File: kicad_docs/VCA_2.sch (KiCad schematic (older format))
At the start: 16 parts, among them U1 SSM2164, U2 TL072, U3 TL072, U4 TL072

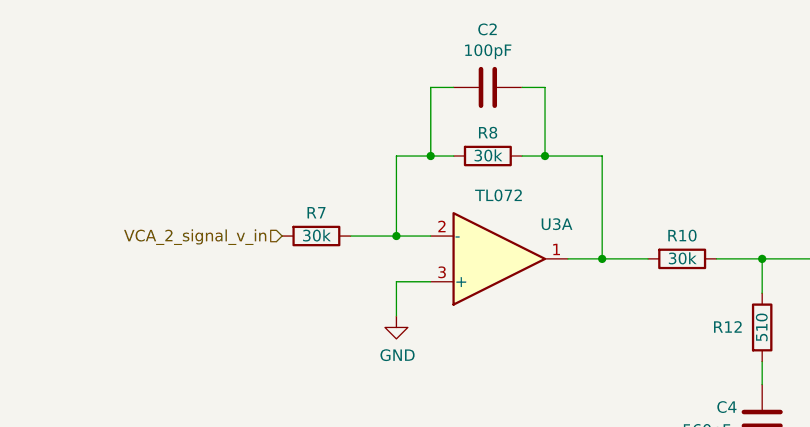
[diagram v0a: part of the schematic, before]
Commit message: add AC/DC coupling caps and jumper
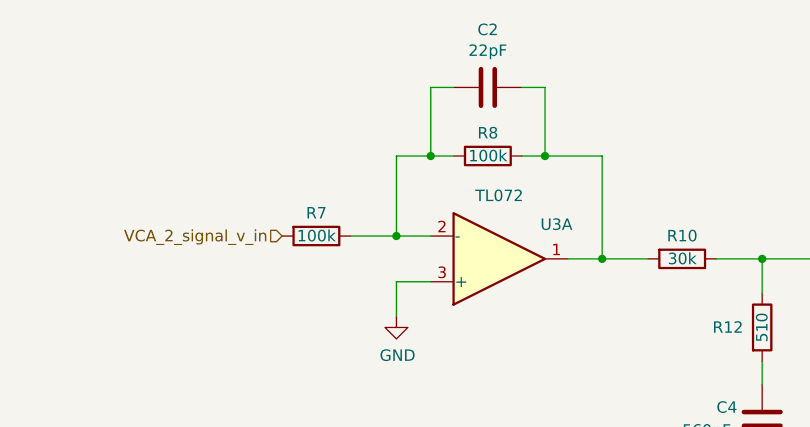
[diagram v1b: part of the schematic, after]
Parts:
- C2: value 100pF -> 22pF
- R7, R8: value 30k -> 100k
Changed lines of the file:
@@
 AR Path="/5E4A03B7/5E985A8F" Ref="R8"  Part="1"
 F 0 "R8" V 4600 2150 50  0000 C CNN
-F 1 "30k" V 4700 2150 50  0000 C CNN
+F 1 "100k" V 4700 2150 50  0000 C CNN
 F 2 "Resistor_SMD:R_0805_2012Metric_Pad1.15x1.40mm_HandSolder" V 4630 2150 50  0001 C CNN
 F 3 "~" H 4700 2150 50  0001 C CNN
@@
 AR Path="/5E4A03B7/5E985AA7" Ref="R7"  Part="1"
 F 0 "R7" V 3850 2500 50  0000 C CNN
-F 1 "30k" V 3950 2500 50  0000 C CNN
+F 1 "100k" V 3950 2500 50  0000 C CNN
 F 2 "Resistor_SMD:R_0805_2012Metric_Pad1.15x1.40mm_HandSolder" V 3880 2500 50  0001 C CNN
 F 3 "~" H 3950 2500 50  0001 C CNN
@@
 AR Path="/5E4A03B7/5E985ABB" Ref="C2"  Part="1"
 F 0 "C2" V 4448 1850 50  0000 C CNN
-F 1 "100pF" V 4539 1850 50  0000 C CNN
+F 1 "22pF" V 4539 1850 50  0000 C CNN
 F 2 "Capacitor_SMD:C_0805_2012Metric_Pad1.15x1.40mm_HandSolder" H 4738 1700 50  0001 C CNN
 F 3 "~" H 4700 1850 50  0001 C CNN

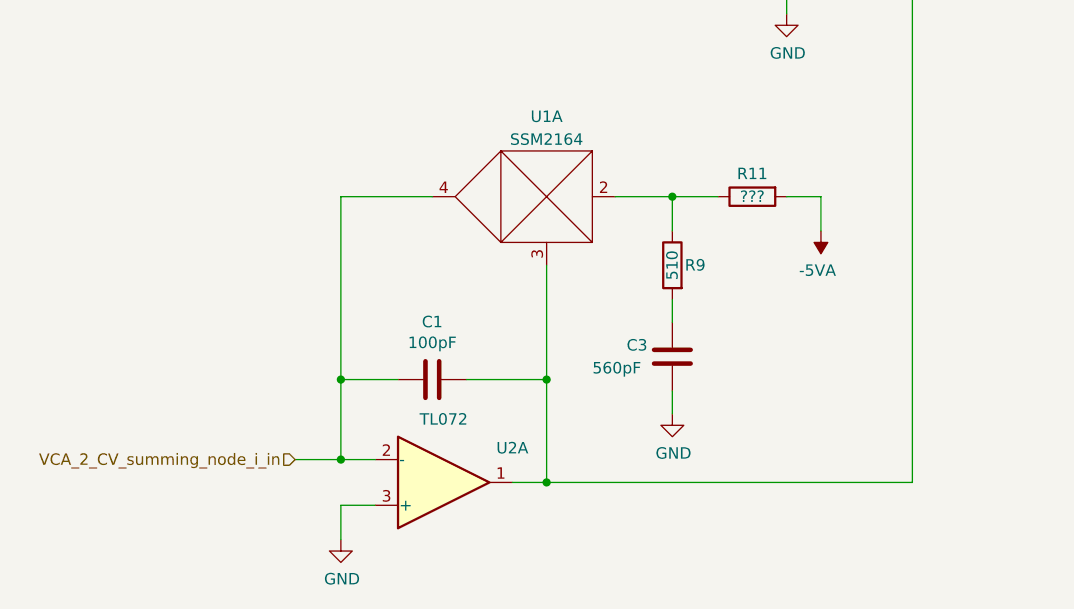
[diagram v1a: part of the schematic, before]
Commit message: add values to r's, add r's to CV circuit
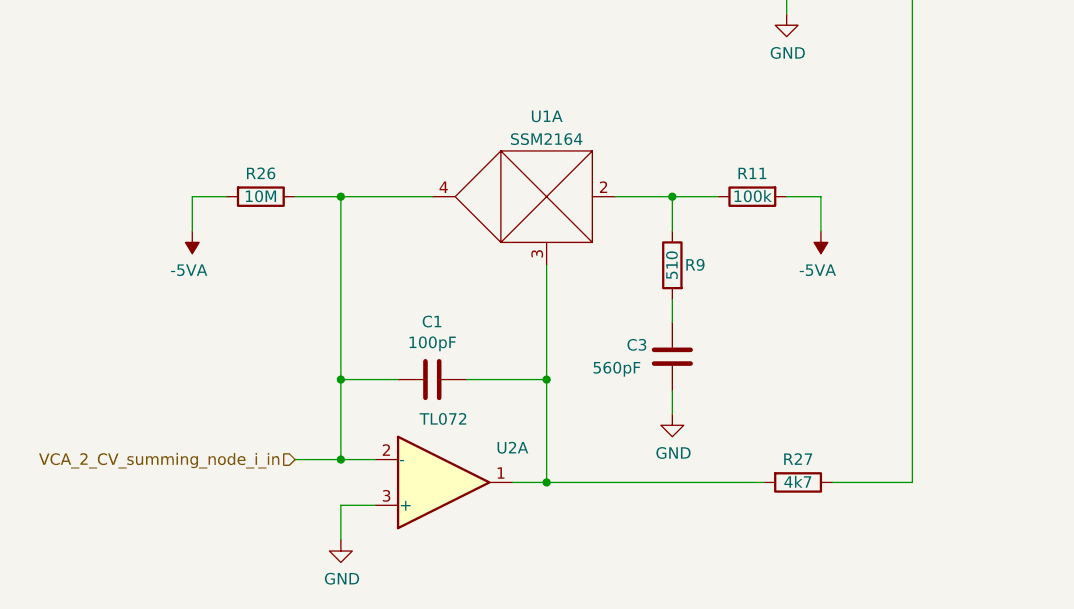
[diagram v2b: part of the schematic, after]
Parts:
- added R26: 10M, Resistor_SMD:R_0805_2012Metric_Pad1.15x1.40mm_HandSolder, symbol Device:R
- added R27: 4k7, Resistor_SMD:R_0805_2012Metric_Pad1.15x1.40mm_HandSolder, symbol Device:R
- R11: value ??? -> 100k
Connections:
- net -5VA: now also R26.2
- net VCA_2_CV_summing_node_i_in: now also R26.1
- net at C1.1, U1.3, U2.1: now also R27.2; no longer U1.6
- new net: R27.1, U1.6
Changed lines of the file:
@@
 AR Path="/5E4A03B7/5E985A4A" Ref="R11"  Part="1"
 F 0 "R11" V 5650 4350 50  0000 C CNN
-F 1 "???" V 5750 4350 50  0000 C CNN
+F 1 "100k" V 5750 4350 50  0000 C CNN
 F 2 "Resistor_SMD:R_0805_2012Metric_Pad1.15x1.40mm_HandSolder" V 5680 4350 50  0001 C CNN
 F 3 "~" H 5750 4350 50  0001 C CNN
@@
 	5400 4900 5400 4800
 Wire Wire Line
-	4850 5600 6450 5600
-Wire Wire Line
 	6450 5600 6450 2900
-Connection ~ 4850 5600
 $Comp
 L Amplifier_Operational:TL072 U?
@@
 Wire Wire Line
 	6050 4350 5900 4350
+$Comp
+L Device:R R27
+U 1 1 5E477841
+P 5950 5600
+F 0 "R27" V 5850 5600 50  0000 C CNN
+F 1 "4k7" V 5950 5600 50  0000 C CNN
+F 2 "Resistor_SMD:R_0805_2012Metric_Pad1.15x1.40mm_HandSolder" V 5880 5600 50  0001 C CNN
+F 3 "~" H 5950 5600 50  0001 C CNN
+	1    5950 5600
+	0    1    1    0
+$EndComp
+$Comp
+L Device:R R26
+U 1 1 5E477BC7
+P 3600 4350
+F 0 "R26" V 3500 4350 50  0000 C CNN
+F 1 "10M" V 3600 4350 50  0000 C CNN
+F 2 "Resistor_SMD:R_0805_2012Metric_Pad1.15x1.40mm_HandSolder" V 3530 4350 50  0001 C CNN
+F 3 "~" H 3600 4350 50  0001 C CNN
+	1    3600 4350
+	0    1    1    0
+$EndComp
+Wire Wire Line
+	6100 5600 6450 5600
+Wire Wire Line
+	5800 5600 4850 5600
+Connection ~ 4850 5600
+$Comp
+L power:-5VA #PWR?
+U 1 1 5E47EFD7
+P 3300 4500
+AR Path="/5E48E312/5E47EFD7" Ref="#PWR?"  Part="1"
+AR Path="/5E4A03B7/5E47EFD7" Ref="#PWR016"  Part="1"
+F 0 "#PWR016" H 3300 4600 50  0001 C CNN
+F 1 "-5VA" H 3315 4673 50  0000 C CNN
+F 2 "" H 3300 4500 50  0001 C CNN
+F 3 "" H 3300 4500 50  0001 C CNN
+	1    3300 4500
+	-1   0    0    1
+$EndComp
+Wire Wire Line
+	3300 4500 3300 4350
+Wire Wire Line
+	3300 4350 3450 4350
+Wire Wire Line
+	3750 4350 3950 4350
+Connection ~ 3950 4350
 $EndSCHEMATC
